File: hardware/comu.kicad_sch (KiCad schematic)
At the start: 18 parts, among them J1 USB_A_Embedded, U1 CH32V203F8U6, U2 XC6206PxxxMR

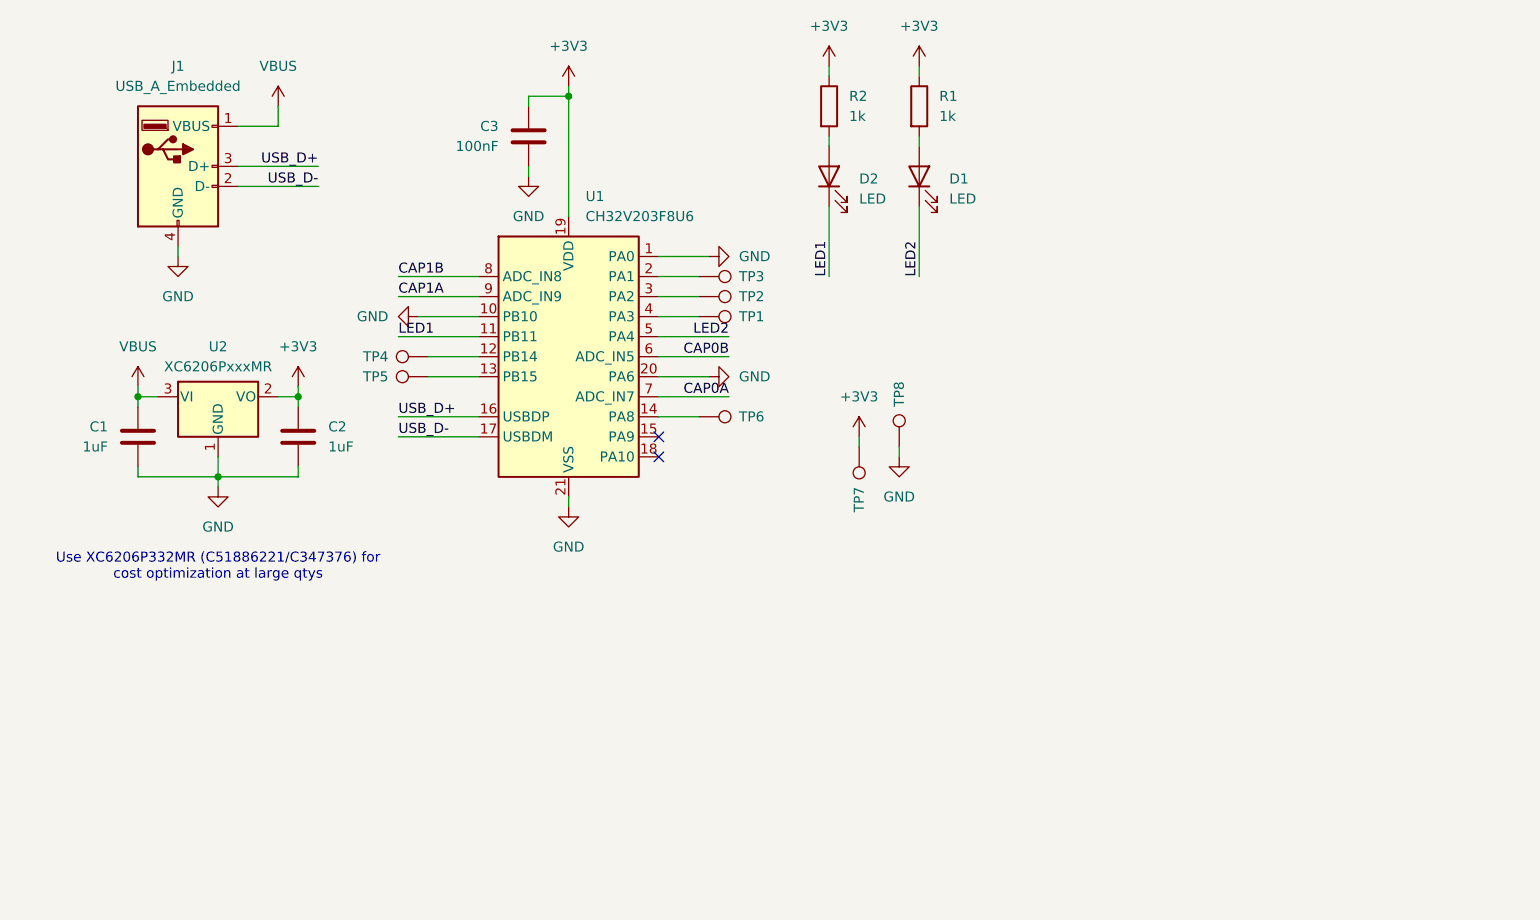
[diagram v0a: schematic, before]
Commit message: Add pdf of schematic and field annotation
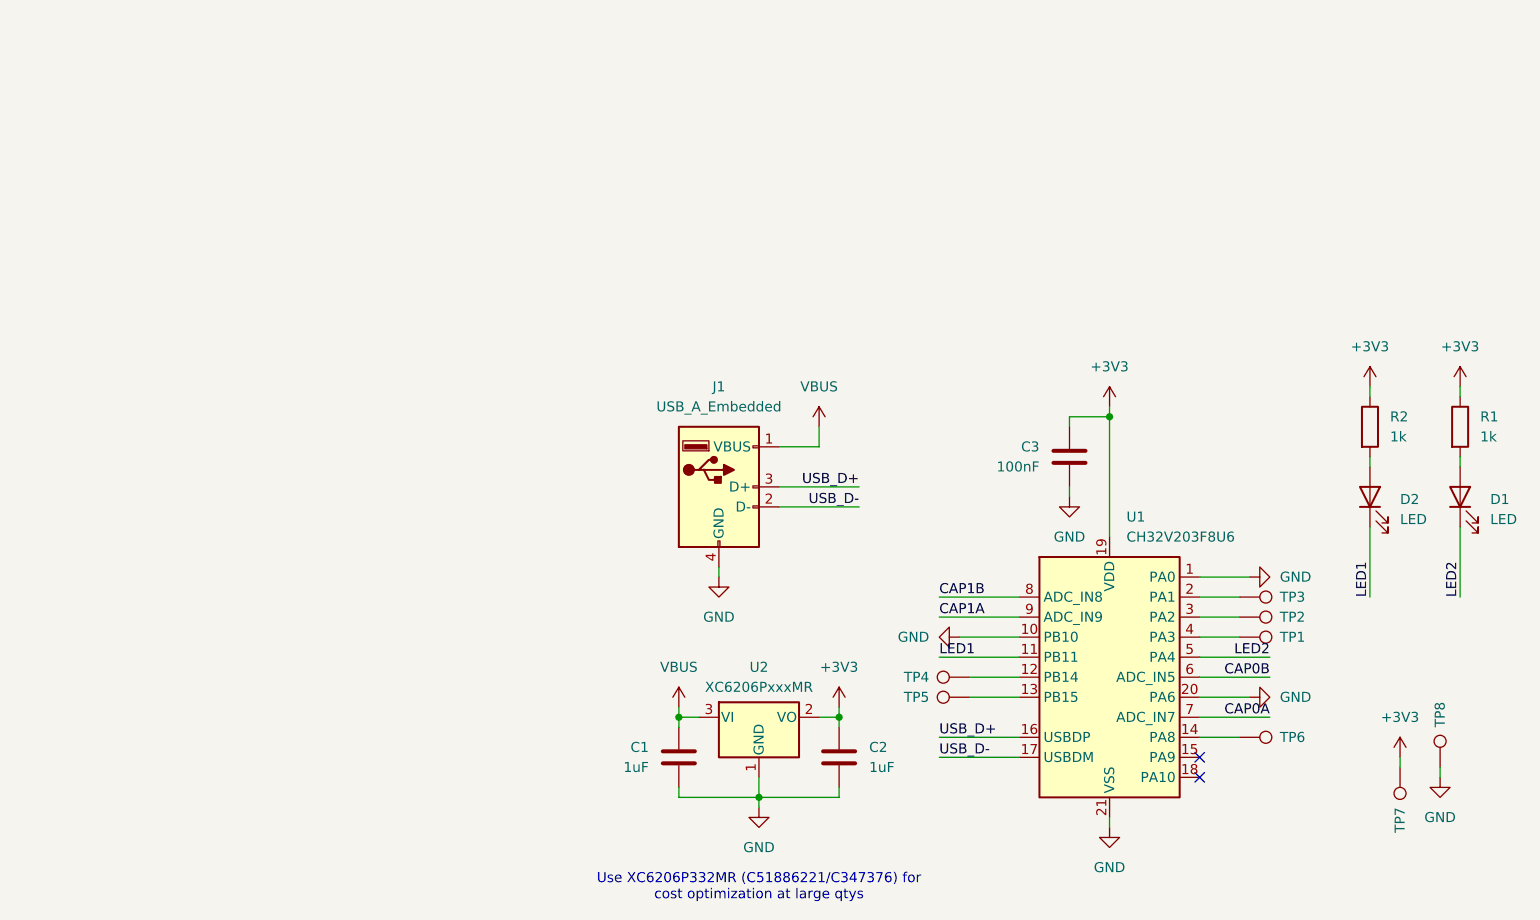
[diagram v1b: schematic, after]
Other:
- company: (none) -> Icy Electronics
- title: (none) -> Comu
- moved on the sheet: C1, C2, C3, D1, D2, J1, R1, R2, TP1, TP2, TP3, TP4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
